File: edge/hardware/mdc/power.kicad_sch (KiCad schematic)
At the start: 1 part, among them J2 Screw_Terminal_01x02

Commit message: rev3.0 schematics
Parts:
- added C2: 10uF, symbol Device:C_Polarized_Small
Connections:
- net +5V: now also C2.1
- net GND: now also C2.2
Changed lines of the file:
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@@
 	(title_block
 		(title "Power")
-		(date "2026-08-08")
+		(date "2026-08-09")
 		(rev "3.0")
 		(comment 1 "Department of EECS- AIoT and Energy Management Lab")
@@
 		(comment 4 "Student: Purit Hongjirakul 黃子奇")
 	)
-	(wire
-		(pts
-			(xy 135.89 100.33) (xy 135.89 99.06)
-		)
-		(stroke
-			(width 0)
-			(type default)
-		)
-	)
-	(wire
-		(pts
-			(xy 135.89 102.87) (xy 137.16 102.87)
-		)
-		(stroke
-			(width 0)
-			(type default)
-		)
-	)
-	(wire
-		(pts
-			(xy 135.89 104.14) (xy 135.89 102.87)
-		)
-		(stroke
-			(width 0)
-			(type default)
-		)
-	)
-	(wire
-		(pts
-			(xy 137.16 100.33) (xy 135.89 100.33)
+	(junction
+		(at 132.08 97.79)
+		(diameter 0)
+		(color 0 0 0 0)
+	)
+	(junction
+		(at 132.08 105.41)
+		(diameter 0)
+		(color 0 0 0 0)
+	)
+	(wire
+		(pts
+			(xy 132.08 106.68) (xy 132.08 105.41)
+		)
+		(stroke
+			(width 0)
+			(type default)
+		)
+	)
+	(wire
+		(pts
+			(xy 132.08 105.41) (xy 132.08 104.14)
+		)
+		(stroke
+			(width 0)
+			(type default)
+		)
+	)
+	(wire
+		(pts
+			(xy 132.08 97.79) (xy 132.08 99.06)
+		)
+		(stroke
+			(width 0)
+			(type default)
+		)
+	)
+	(wire
+		(pts
+			(xy 137.16 105.41) (xy 137.16 102.87)
+		)
+		(stroke
+			(width 0)
+			(type default)
+		)
+	)
+	(wire
+		(pts
+			(xy 132.08 105.41) (xy 137.16 105.41)
+		)
+		(stroke
+			(width 0)
+			(type default)
+		)
+	)
+	(wire
+		(pts
+			(xy 137.16 97.79) (xy 132.08 97.79)
+		)
+		(stroke
+			(width 0)
+			(type default)
+		)
+	)
+	(wire
+		(pts
+			(xy 137.16 97.79) (xy 137.16 100.33)
+		)
+		(stroke
+			(width 0)
+			(type default)
+		)
+	)
+	(wire
+		(pts
+			(xy 132.08 96.52) (xy 132.08 97.79)
 		)
 		(stroke
@@
 	(symbol
 		(lib_id "power:GND")
-		(at 135.89 104.14 0)
+		(at 132.08 106.68 0)
 		(unit 1)
 		(body_style 1)
@@
 		(fields_autoplaced yes)
 		(property "Reference" "#PWR023"
-			(at 135.89 110.49 0)
+			(at 132.08 113.03 0)
 			(hide yes)
 			(show_name no)
@@
 		)
 		(property "Value" "GND"
-			(at 135.89 109.22 0)
+			(at 132.08 111.76 0)
 			(show_name no)
 			(do_not_autoplace no)
@@
 		)
 		(property "Footprint" ""
-			(at 135.89 104.14 0)
+			(at 132.08 106.68 0)
 			(hide yes)
 			(show_name no)
@@
 		)
 		(property "Datasheet" ""
-			(at 135.89 104.14 0)
+			(at 132.08 106.68 0)
 			(hide yes)
 			(show_name no)
@@
 		)
 		(property "Description" "Power symbol creates a global label with name \"GND\" , ground"
-			(at 135.89 104.14 0)
+			(at 132.08 106.68 0)
 			(hide yes)
 			(show_name no)
@@
 	)
 	(symbol
+		(lib_id "Device:C_Polarized_Small")
+		(at 132.08 101.6 0)
+		(mirror y)
+		(unit 1)
+		(body_style 1)
+		(exclude_from_sim no)
+		(in_bom yes)
+		(on_board yes)
+		(in_pos_files yes)
+		(dnp no)
+		(property "Reference" "C2"
+			(at 130.048 100.3682 0)
+			(show_name no)
+			(do_not_autoplace no)
+			(effects
+				(font
+					(size 1.27 1.27)
+				)
+				(justify left)
+			)
+		)
+		(property "Value" "10uF"
+			(at 130.048 102.616 0)
+			(show_name no)
+			(do_not_autoplace no)
+			(effects
+				(font
+					(size 1.27 1.27)
+				)
+				(justify left)
+			)
+		)
+		(property "Footprint" ""
+			(at 132.08 101.6 0)
+			(hide yes)
+			(show_name no)
+			(do_not_autoplace no)
+			(effects
+				(font
+					(size 1.27 1.27)
+				)
+			)
+		)
+		(property "Datasheet" ""
+			(at 132.08 101.6 0)
+			(hide yes)
+			(show_name no)
+			(do_not_autoplace no)
+			(effects
+				(font
+					(size 1.27 1.27)
+				)
+			)
+		)
+		(property "Description" "Polarized capacitor"
+			(at 132.08 101.6 0)
+			(hide yes)
+			(show_name no)
+			(do_not_autoplace no)
+			(effects
+				(font
+					(size 1.27 1.27)
+				)
+			)
+		)
+		(pin "1"
+		)
+		(pin "2"
+		)
+		(instances
+			(project "mdc"
+				(path "/813130ed-0e1e-452d-b14e-fae57783a961/747a2106-db37-4aed-b41f-3c0ea0387f8e"
+					(reference "C2")
+					(unit 1)
+				)
+			)
+		)
+	)
+	(symbol
 		(lib_id "power:+5V")
-		(at 135.89 99.06 0)
+		(at 132.08 96.52 0)
 		(unit 1)
 		(body_style 1)
@@
 		(fields_autoplaced yes)
 		(property "Reference" "#PWR022"
-			(at 135.89 102.87 0)
+			(at 132.08 100.33 0)
 			(hide yes)
 			(show_name no)
@@
 		)
 		(property "Value" "+5V"
-			(at 135.89 93.98 0)
+			(at 132.08 91.44 0)
 			(show_name no)
 			(do_not_autoplace no)
@@
 		)
 		(property "Footprint" ""
-			(at 135.89 99.06 0)
+			(at 132.08 96.52 0)
 			(hide yes)
 			(show_name no)
@@
 		)
 		(property "Datasheet" ""
-			(at 135.89 99.06 0)
+			(at 132.08 96.52 0)
 			(hide yes)
 			(show_name no)
@@
 		)
 		(property "Description" "Power symbol creates a global label with name \"+5V\""
-			(at 135.89 99.06 0)
-			(hide yes)
-			(show_name no)
+			(at 132.08 96.52 0)
+			(hide yes)
+			(show_name no)

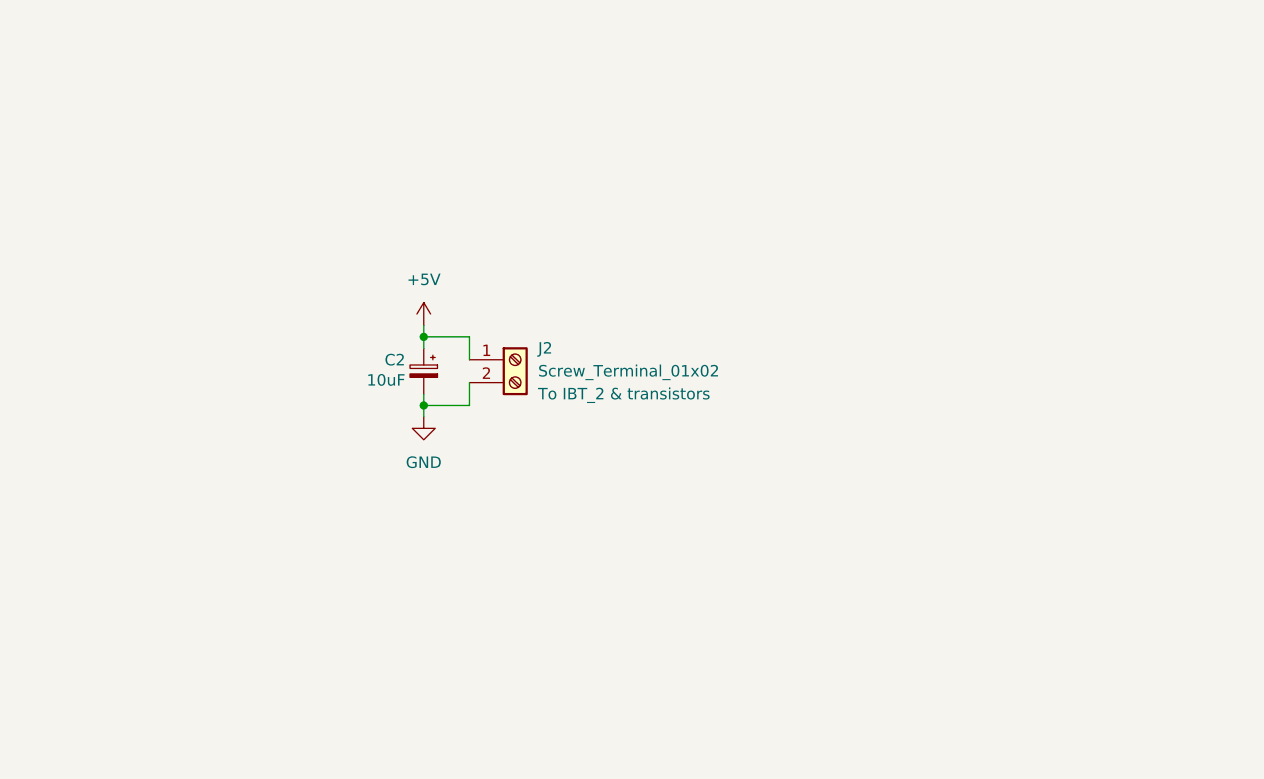
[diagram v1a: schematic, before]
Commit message: finish rev3.0 PCB layout + data collector script changes + firmware changes
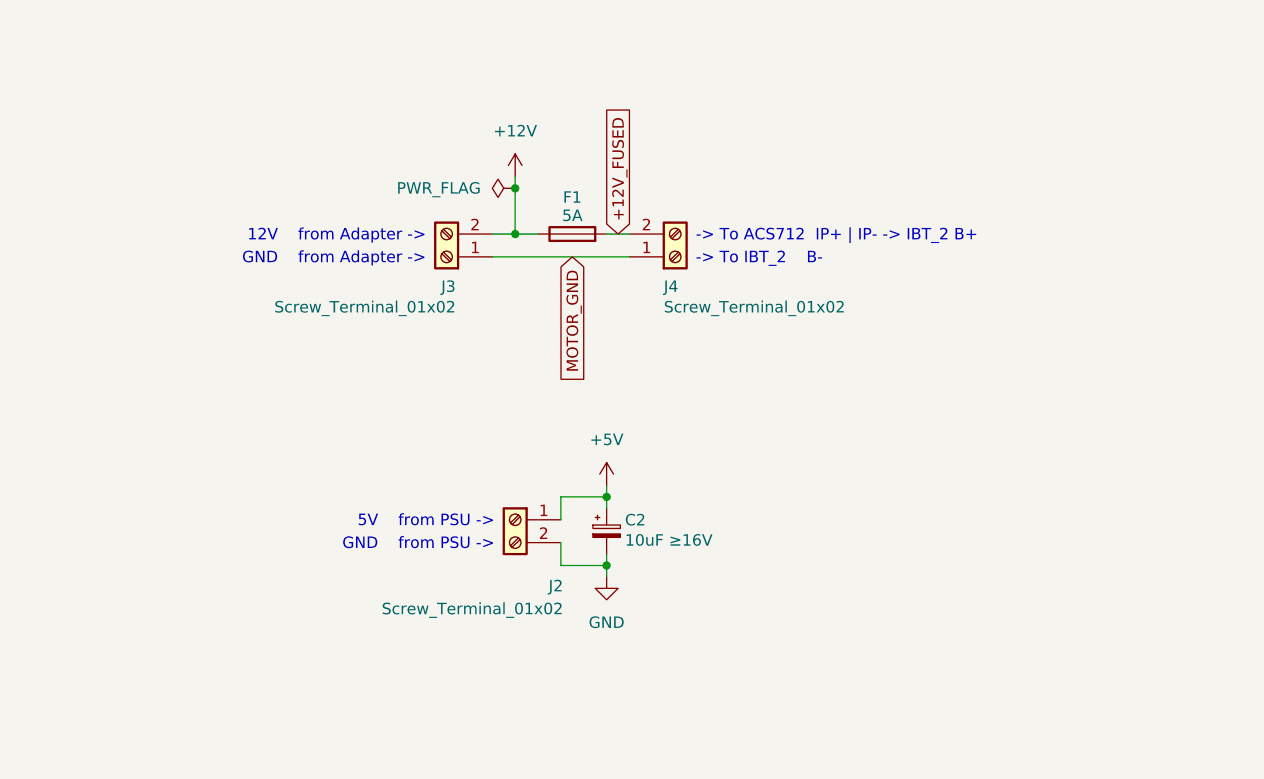
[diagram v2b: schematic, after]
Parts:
- added F1: 5A, Fuse:Fuseholder_Cylinder-5x20mm_Schurter_0031_8201_Horizontal_Open, symbol Device:Fuse
- added J3, J4: Screw_Terminal_01x02, TerminalBlock_Altech:Altech_AK100_1x02_P5.00mm, symbol Connector:Screw_Terminal_01x02
- C2: value 10uF -> 10uF ≥16V; footprint (none) -> Capacitor_THT:CP_Radial_D5.0mm_P2.50mm
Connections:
- new net +12V: F1.1, J3.2 (Pin_2)
- new net +12V_FUSED: F1.2, J4.2 (Pin_2)
- new net MOTOR_GND: J3.1 (Pin_1), J4.1 (Pin_1)
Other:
- note added: "-> To ACS712 IP+ | IP- -> IBT_2 B+"
- note added: "-> To IBT_2 B-"
- note added: "12V from Adapter ->"
- note added: "5V from PSU ->"
- note added: "GND from Adapter ->"
- note added: "GND from PSU ->"
- moved on the sheet: C2, J2

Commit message: update rev3.0 schematic and layout
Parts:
- added C10: 470uF 25V, Capacitor_THT:CP_Radial_D5.0mm_P2.50mm, symbol Device:C_Polarized_Small
- added D1: 10V 1W, Diode_THT:D_DO-41_SOD81_P7.62mm_Horizontal, symbol Device:D_Zener_Small
- added Q5: IRF4905, Package_TO_SOT_THT:TO-220-3_Vertical, symbol Transistor_FET:IRF4905
- added Q6: NDP6020P, Package_TO_SOT_THT:TO-220-3_Vertical, symbol Transistor_FET:IRF4905
- added R14, R15: 100k, Resistor_THT:R_Axial_DIN0207_L6.3mm_D2.5mm_P7.62mm_Horizontal, symbol Device:R_Small
- C2: value 10uF ≥16V -> 10uF 16V
- F1: value 5A -> 6A
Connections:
- net +12V: now also D1.1 (K), Q5.3 (S); no longer F1.1
- net +12V_FUSED: now also C10.1
- net +5V: now also Q6.2 (D); no longer J2.1 (Pin_1)
- net GND: now also R15.2
- net MOTOR_GND: now also C10.2, R14.2
- new net: D1.2 (A), Q5.1 (G), R14.1
- new net: J2.1 (Pin_1), Q6.3 (S)
- new net: Q6.1 (G), R15.1
- new net: F1.1, Q5.2 (D)
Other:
- moved on the sheet: C2, F1, J2, J3, J4

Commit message: update rev3.0 schematic and layout
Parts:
- removed D1: 10V 1W, Diode_THT:D_DO-41_SOD81_P7.62mm_Horizontal, symbol Device:D_Zener_Small
- removed J2, J3, J4: Screw_Terminal_01x02, TerminalBlock_Altech:Altech_AK100_1x02_P5.00mm, symbol Connector:Screw_Terminal_01x02
- removed Q5: IRF4905, Package_TO_SOT_THT:TO-220-3_Vertical, symbol Transistor_FET:IRF4905
- removed Q6: NDP6020P, Package_TO_SOT_THT:TO-220-3_Vertical, symbol Transistor_FET:IRF4905
- added J2, J3, J4: Conn_01x02, Connector_JST:JST_VH_B2P-VH-B_1x02_P3.96mm_Vertical, symbol Connector_Generic:Conn_01x02
- added Q5: IRFZ44N, Package_TO_SOT_THT:TO-220-3_Vertical, symbol Transistor_FET:IRF540N
- C10: footprint Capacitor_THT:CP_Radial_D5.0mm_P2.50mm -> Capacitor_THT:CP_Radial_D8.0mm_P3.50mm
- R15: value 100k -> 10k
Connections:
- net +12V: now also F1.1, R15.2, J3.2 (Pin_2)
- net +12V_FUSED: now also J4.1 (Pin_1)
- net +5V: now also J2.2 (Pin_2)
- net GND: now also J2.1 (Pin_1); no longer R15.2
- net MOTOR_GND: now also J4.2 (Pin_2), Q5.3 (S)
- net at R14.1: now also R15.1, Q5.1 (G)
- new net: J3.1 (Pin_1), Q5.2 (D)
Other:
- moved on the sheet: C10, C2, F1, R14

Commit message: added rev3.1 + some ML adjustments
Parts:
- removed Q5: IRFZ44N, Package_TO_SOT_THT:TO-220-3_Vertical, symbol Transistor_FET:IRF540N
- removed R14: 100k, Resistor_THT:R_Axial_DIN0207_L6.3mm_D2.5mm_P7.62mm_Horizontal, symbol Device:R_Small
- removed R15: 10k, Resistor_THT:R_Axial_DIN0207_L6.3mm_D2.5mm_P7.62mm_Horizontal, symbol Device:R_Small
- F1: value 6A -> T10A
- J2, J3, J4: footprint Connector_JST:JST_VH_B2P-VH-B_1x02_P3.96mm_Vertical -> TerminalBlock:TerminalBlock_MaiXu_MX126-5.0-02P_1x02_P5.00mm
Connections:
- net MOTOR_GND: now also J3.1 (Pin_1)
